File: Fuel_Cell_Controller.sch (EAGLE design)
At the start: 31 parts, among them U1 MAX232PTH

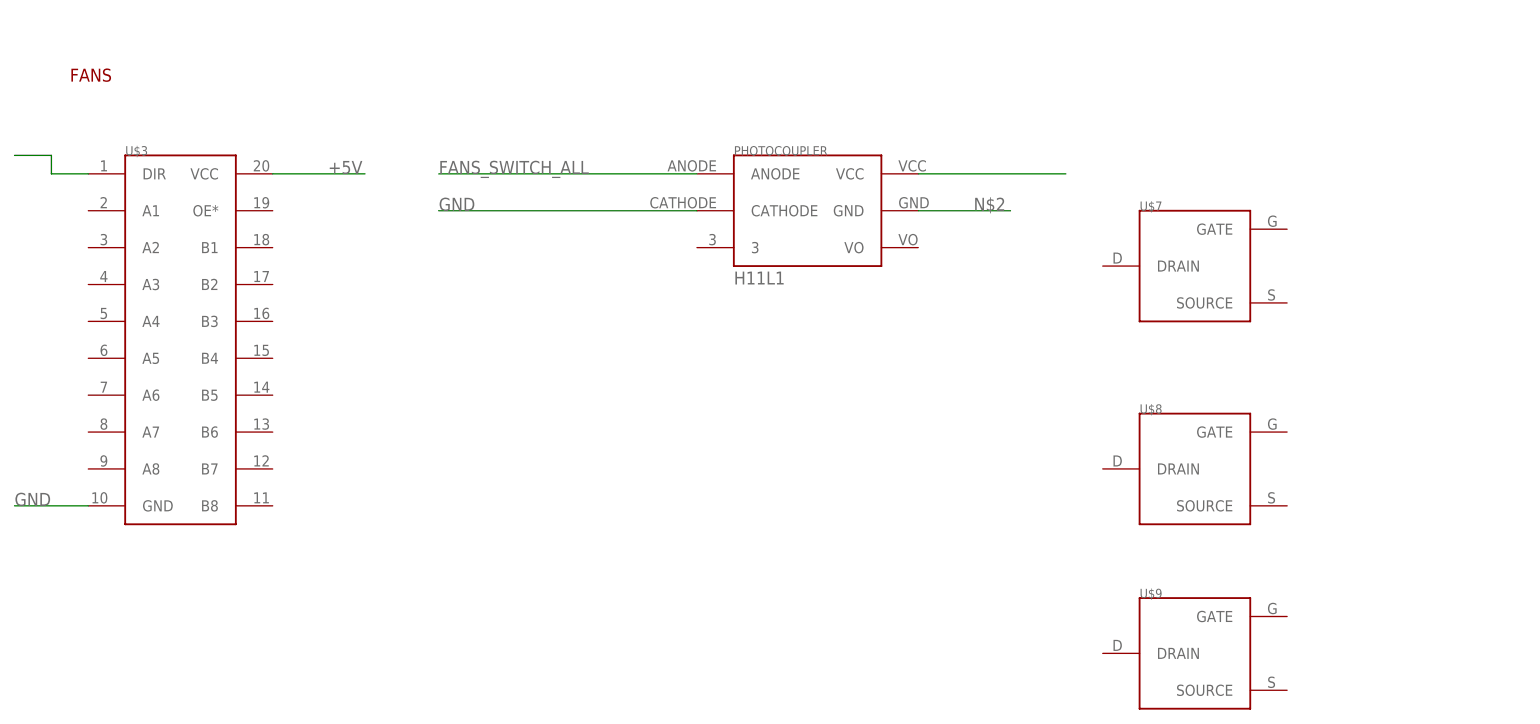
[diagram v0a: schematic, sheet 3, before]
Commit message: Added photocouplers
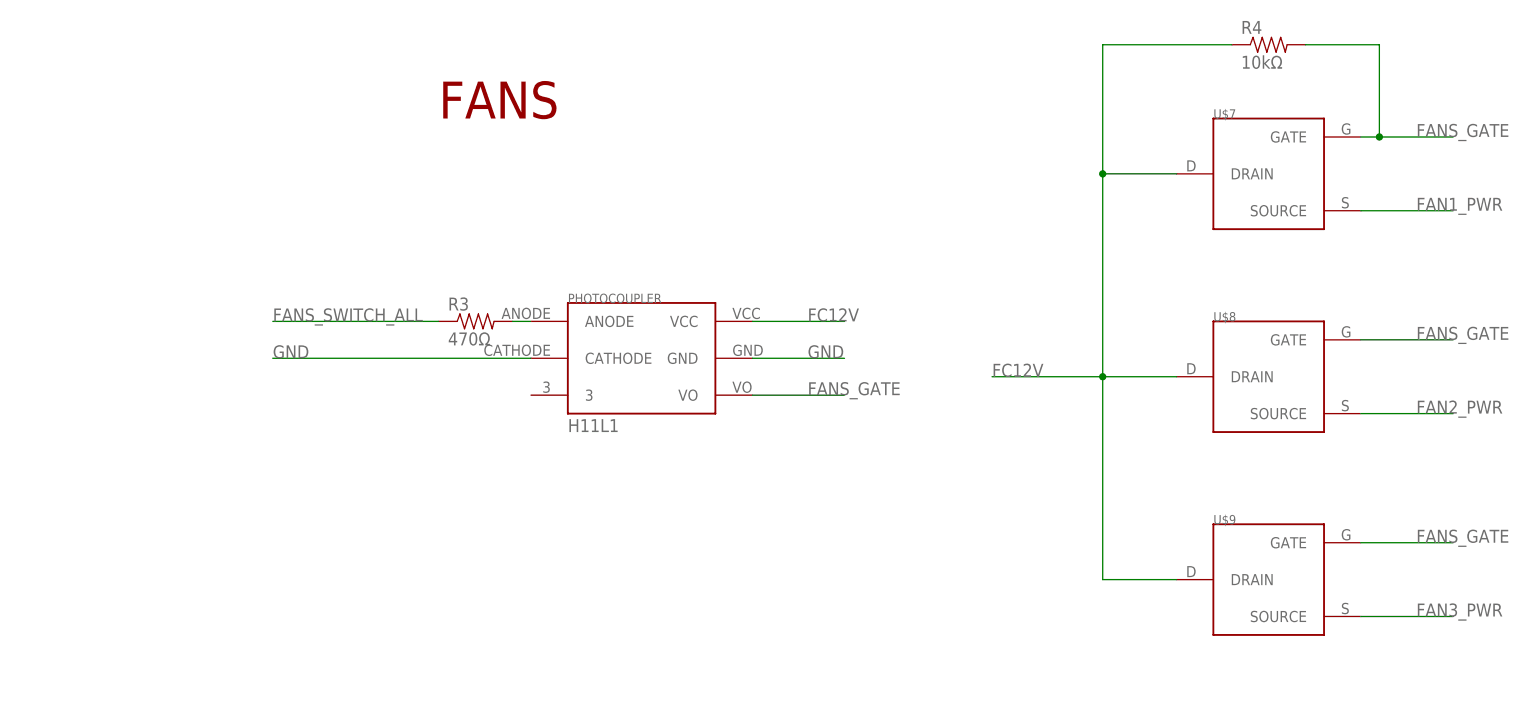
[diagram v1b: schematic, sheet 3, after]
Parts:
- added R10, R12, R4, R6, R8: 10kΩ, SparkFun-Resistors:RESISTOR0603
- added R11, R3, R5, R7, R9: 470Ω, SparkFun-Resistors:RESISTOR0603
- added R2: 1kΩ, SparkFun-Resistors:RESISTOR0603
- added U$11, U$14, U$16, U$6: H11L1H11L1, FCC_parts:H11L1H11L1
- added U$12, U$13, U$15, U$17: DMP3056L-7DMP3056L-7, FCC_parts:DMP3056L-7DMP3056L-7
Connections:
- removed net FANS_SWITCH_1: ETH7.1
- removed net FANS_SWITCH_2: ETH7.4
- removed net FANS_SWITCH_3: ETH8.1
- new net FAN1_PWR: ETH7.1, U$7.SOURCE
- new net FAN2_PWR: ETH7.4, U$8.SOURCE
- new net FAN3_PWR: ETH8.1, U$9.SOURCE
- new net FANS_GATE: R4.2, U$4.VO, U$7.GATE, U$8.GATE, U$9.GATE
- new net N$12: R3.2, U$4.ANODE
- new net N$13: R9.2, U$14.ANODE
- new net N$14: R11.2, U$16.ANODE
- new net OUTPUT_1_ENET: ETH9.5, U$15.SOURCE
- new net OUTPUT_1_GATE: R10.2, U$14.VO, U$15.GATE
- new net OUTPUT_2_ENET: ETH9.7, U$17.SOURCE
- new net OUTPUT_2_GATE: R12.2, U$16.VO, U$17.GATE
- new net PURGE_VALVE_ENET: ETH9.3, U$13.SOURCE
- new net PURGE_VALVE_GATE: R8.2, U$11.VO, U$13.GATE
- new net SUPPLY_VALVE_ENET: ETH9.1, U$12.SOURCE
- new net SUPPLY_VALVE_GATE: R6.2, U$12.GATE, U$6.VO
- new net _FANS_SWITCH_ALL: U$1.PE_3, U$3.A1
- new net _OUTPUT_1: U$1.PD_0(CAN1_RD), U$3.A4
- new net _OUTPUT_2: U$1.PD_1(CAN1_TD), U$3.A5
- new net _PURGE_VALVE: U$1.PC_11(SERIAL4_RX/SPI3_MISO), U$3.A3
- new net _SUPPLY_VALVE: U$1.PC_10(SERIAL3_TX/SPI3_SCLK), U$3.A2
- net +5V: now also R2.1
- net FANS_SWITCH_ALL: now also R3.1, U$3.B1; no longer U$1.PE_3, U$4.ANODE
- net FC12V: now also R10.1, R12.1, R4.1, R6.1, R8.1, U$11.VCC, U$12.DRAIN, U$13.DRAIN, U$14.VCC, U$15.DRAIN, U$16.VCC, U$17.DRAIN, U$4.VCC, U$6.VCC, U$7.DRAIN, U$8.DRAIN, U$9.DRAIN
- net GND: now also U$11.CATHODE, U$11.GND, U$14.CATHODE, U$14.GND, U$16.CATHODE, U$16.GND, U$4.GND, U$6.CATHODE, U$6.GND
- net N$10: now also R2.2
- net N$2: now also R5.2, U$6.ANODE; no longer U$4.GND
- net N$9: now also R7.2, U$11.ANODE; no longer U$4.VCC
- net OUTPUT_1: now also R9.1, U$3.B4; no longer ETH9.5, U$1.PD_0(CAN1_RD)
- net OUTPUT_2: now also R11.1, U$3.B5; no longer ETH9.7, U$1.PD_1(CAN1_TD)
- net PURGE_VALVE: now also R7.1, U$3.B3; no longer ETH9.3, U$1.PC_11(SERIAL4_RX/SPI3_MISO)
- net SUPPLY_VALVE: now also R5.1, U$3.B2; no longer ETH9.1, U$1.PC_10(SERIAL3_TX/SPI3_SCLK)
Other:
- moved on the sheet: U$7, U$8, U$9

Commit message: Added rs232 to mass flow meter
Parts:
- removed ETH5: ETHERNET, ETHERNET:ETHERNET
- added X1: (no value), con-subd:F09HP
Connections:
- removed net N$61: ETH5.2
- removed net N$62: ETH5.3
- removed net N$63: ETH5.4
- removed net N$64: ETH5.5
- removed net N$65: ETH5.7
- removed net N$66: ETH5.6
- removed net N$96: ETH1.7
- new net AGND: ETH1.7, ETH4.8, U$1.AGND, X1.2
- new net MASS_FLOW: X1.3
- net FC12V: now also X1.4; no longer ETH5.1
- net GND: now also X1.5; no longer ETH4.8, ETH5.8, ETH5.SHD1, ETH5.SHD2, U$1.AGND
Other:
- note added: "RS232 TO MASS FLOW METER"
- note removed: "Mass Flow Connector"
- moved on the sheet: ETH6, ETH7, ETH8, ETH9

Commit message: Added DS3231 RTC
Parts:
- added C6: (no value), SparkFun-Capacitors:CAP0603-CAP
- added R13, R14: 10kΩ, SparkFun-Resistors:RESISTOR0603
- added U$18: DS3231, DS3231:DS3231
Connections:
- new net I2C1_SDA: R14.2, U$1.PB_9(D14/CAN1_TD/SPI2_SSEL/I2C1_SDA/PWM4/4), U$18.SDA
- net 3V3: now also C6.1, R13.1, R14.1, U$18.3.3V
- net GND: now also C6.2, U$18.GND
- net I2C1_SCL: now also R13.2, U$18.SCL
- net ISC1_SDA: no longer U$1.PB_9(D14/CAN1_TD/SPI2_SSEL/I2C1_SDA/PWM4/4)
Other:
- note added: "REAL TIME CLOCK"
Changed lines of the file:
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@@
 <part name="R12" library="SparkFun-Resistors" deviceset="RESISTOR" device="0603" value="10kΩ"/>
 <part name="X1" library="con-subd" library_urn="urn:adsk.eagle:library:189" deviceset="F09" device="HP" package3d_urn="urn:adsk.eagle:package:10232/1"/>
+<part name="U$18" library="DS3231" deviceset="DS3231" device=""/>
+<part name="R13" library="SparkFun-Resistors" deviceset="RESISTOR" device="0603" value="10kΩ"/>
+<part name="R14" library="SparkFun-Resistors" deviceset="RESISTOR" device="0603" value="10kΩ"/>
+<part name="C6" library="SparkFun-Capacitors" deviceset="CAP" device="0603-CAP"/>
+<part name="GND4" library="E-P-008-R1.2" deviceset="GND" device=""/>
 </parts>
 <sheets>
@@
 <text x="215.9" y="-25.4" size="3.81" layer="94">TEMP/HUMID SENSOR</text>
 <wire x1="210.82" y1="-96.52" x2="281.94" y2="-96.52" width="0.1524" layer="94"/>
-<wire x1="281.94" y1="-96.52" x2="281.94" y2="-15.24" width="0.1524" layer="94"/>
+<wire x1="281.94" y1="-96.52" x2="281.94" y2="-33.02" width="0.1524" layer="94"/>
 <text x="271.78" y="68.58" size="3.81" layer="94">RS232 TO MASS FLOW METER</text>
+<wire x1="281.94" y1="-33.02" x2="281.94" y2="-15.24" width="0.1524" layer="94"/>
 <wire x1="264.16" y1="78.74" x2="360.68" y2="78.74" width="0.1524" layer="94"/>
 <wire x1="360.68" y1="78.74" x2="360.68" y2="33.02" width="0.1524" layer="94"/>
 <wire x1="360.68" y1="33.02" x2="281.94" y2="33.02" width="0.1524" layer="94"/>
+<wire x1="360.68" y1="33.02" x2="360.68" y2="-33.02" width="0.1524" layer="94"/>
+<wire x1="360.68" y1="-33.02" x2="281.94" y2="-33.02" width="0.1524" layer="94"/>
+<text x="294.64" y="22.86" size="3.81" layer="94">REAL TIME CLOCK</text>
 </plain>
 <instances>
@@
 <instance part="R2" gate="G$1" x="17.78" y="-81.28"/>
 <instance part="X1" gate="G$1" x="299.72" y="50.8"/>
+<instance part="U$18" gate="G$1" x="342.9" y="-2.54"/>
+<instance part="R13" gate="G$1" x="309.88" y="5.08"/>
+<instance part="R14" gate="G$1" x="309.88" y="0"/>
+<instance part="C6" gate="G$1" x="294.64" y="-12.7"/>
+<instance part="GND4" gate="1" x="294.64" y="-25.4"/>
 </instances>
 <busses>
@@
 <wire x1="-71.12" y1="33.02" x2="-99.06" y2="33.02" width="0.1524" layer="91"/>
 <label x="-99.06" y="33.02" size="1.778" layer="95"/>
+</segment>
+<segment>
+<pinref part="U$18" gate="G$1" pin="GND"/>
+<wire x1="337.82" y1="10.16" x2="320.04" y2="10.16" width="0.1524" layer="91"/>
+<label x="320.04" y="10.16" size="1.778" layer="95"/>
+</segment>
+<segment>
+<pinref part="C6" gate="G$1" pin="2"/>
+<wire x1="294.64" y1="-15.24" x2="294.64" y2="-22.86" width="0.1524" layer="91"/>
+<pinref part="GND4" gate="1" pin="GND"/>
 </segment>
 </net>
@@
 <label x="-99.06" y="45.72" size="1.778" layer="95"/>
 </segment>
+<segment>
+<pinref part="U$18" gate="G$1" pin="3.3V"/>
+<wire x1="337.82" y1="15.24" x2="320.04" y2="15.24" width="0.1524" layer="91"/>
+<label x="320.04" y="15.24" size="1.778" layer="95"/>
+</segment>
+<segment>
+<pinref part="R14" gate="G$1" pin="1"/>
+<wire x1="304.8" y1="0" x2="299.72" y2="0" width="0.1524" layer="91"/>
+<wire x1="299.72" y1="0" x2="299.72" y2="2.54" width="0.1524" layer="91"/>
+<wire x1="299.72" y1="2.54" x2="294.64" y2="2.54" width="0.1524" layer="91"/>
+<pinref part="R13" gate="G$1" pin="1"/>
+<wire x1="294.64" y1="2.54" x2="289.56" y2="2.54" width="0.1524" layer="91"/>
+<wire x1="304.8" y1="5.08" x2="299.72" y2="5.08" width="0.1524" layer="91"/>
+<wire x1="299.72" y1="5.08" x2="299.72" y2="2.54" width="0.1524" layer="91"/>
+<junction x="299.72" y="2.54"/>
+<label x="289.56" y="2.54" size="1.778" layer="95"/>
+<pinref part="C6" gate="G$1" pin="1"/>
+<wire x1="294.64" y1="2.54" x2="294.64" y2="-7.62" width="0.1524" layer="91"/>
+<junction x="294.64" y="2.54"/>
+</segment>
 </net>
 <net name="OPEN_RST" class="0">
@@
 <label x="-99.06" y="-10.16" size="1.778" layer="95"/>
 </segment>
+<segment>
+<pinref part="U$18" gate="G$1" pin="SCL"/>
+<pinref part="R13" gate="G$1" pin="2"/>
+<wire x1="337.82" y1="5.08" x2="314.96" y2="5.08" width="0.1524" layer="91"/>
+<label x="320.04" y="5.08" size="1.778" layer="95"/>
+</segment>
 </net>
 <net name="ISC1_SDA" class="0">
-<segment>
-<pinref part="U$1" gate="G$1" pin="PB_9(D14/CAN1_TD/SPI2_SSEL/I2C1_SDA/PWM4/4)"/>
-<wire x1="-71.12" y1="-12.7" x2="-99.06" y2="-12.7" width="0.1524" layer="91"/>
-<label x="-99.06" y="-12.7" size="1.778" layer="95"/>
-</segment>
 <segment>
 <pinref part="SHTSENSOR" gate="G$1" pin="SDA"/>
@@
 </segment>
 </net>
+<net name="I2C1_SDA" class="0">
+<segment>
+<pinref part="U$18" gate="G$1" pin="SDA"/>
+<wire x1="337.82" y1="0" x2="314.96" y2="0" width="0.1524" layer="91"/>
+<label x="320.04" y="0" size="1.778" layer="95"/>
+<pinref part="R14" gate="G$1" pin="2"/>
+</segment>
+<segment>
+<pinref part="U$1" gate="G$1" pin="PB_9(D14/CAN1_TD/SPI2_SSEL/I2C1_SDA/PWM4/4)"/>
+<wire x1="-71.12" y1="-12.7" x2="-99.06" y2="-12.7" width="0.1524" layer="91"/>
+<label x="-99.06" y="-12.7" size="1.778" layer="95"/>
+</segment>
+</net>

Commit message: Made it look prettier
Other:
- note added: "OUTPUT BUFFERS"
